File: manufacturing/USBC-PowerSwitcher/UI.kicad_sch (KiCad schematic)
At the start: 1 part, among them SW1 EC11N152440x

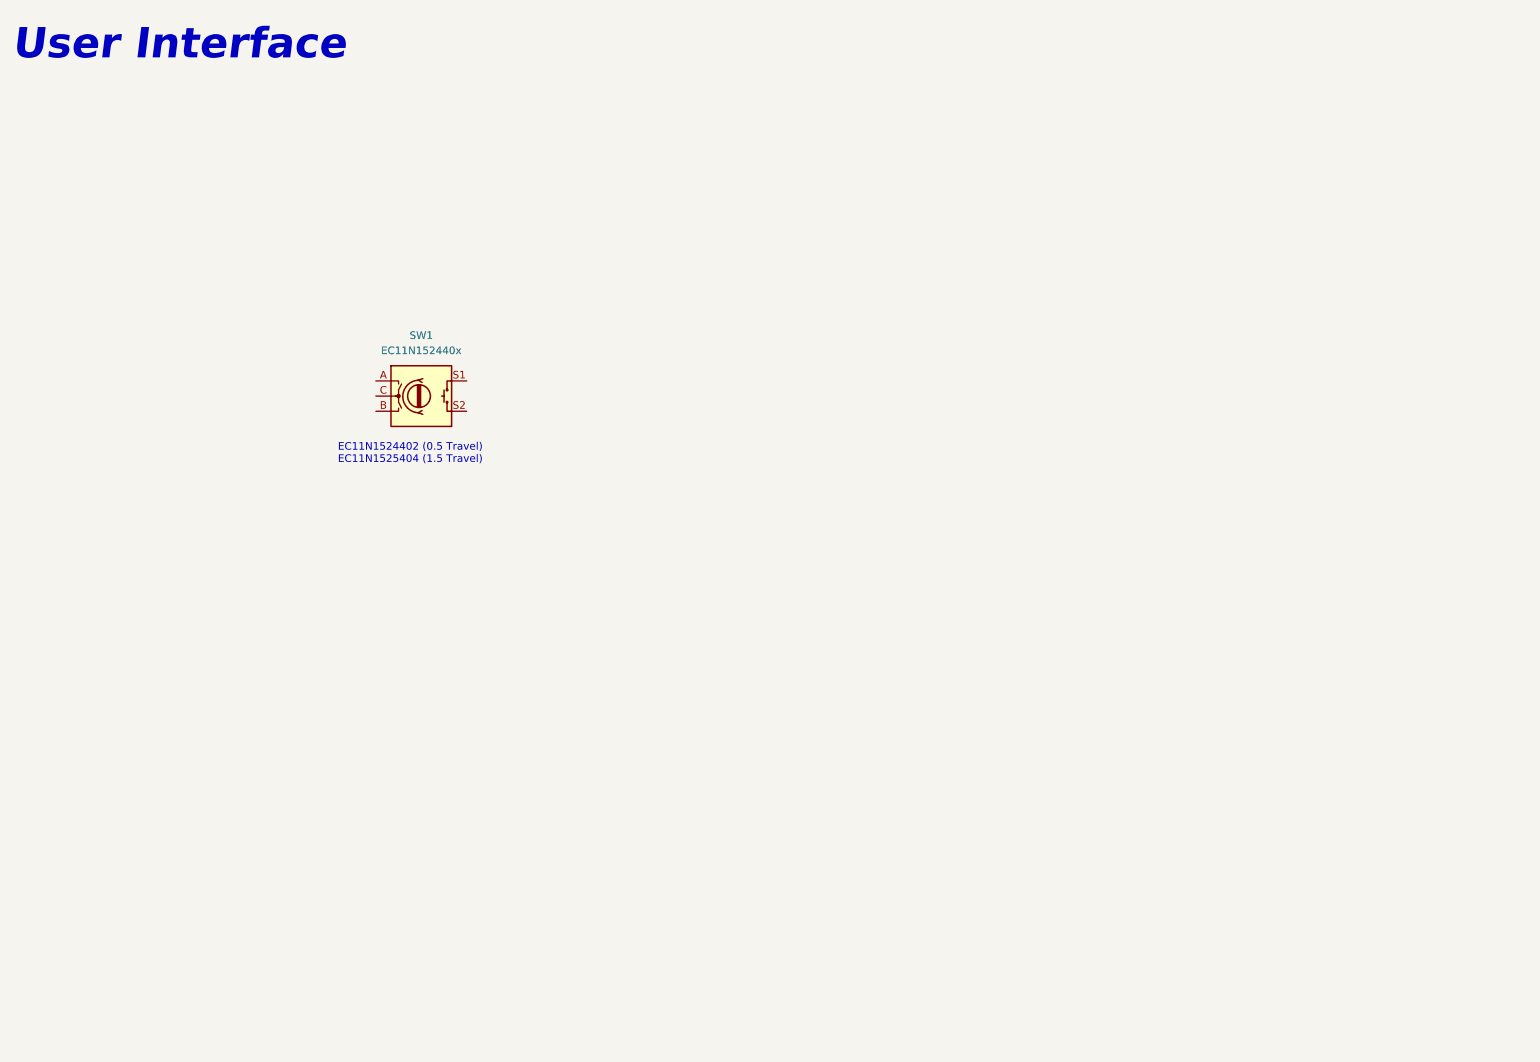
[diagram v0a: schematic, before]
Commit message: First Rough placement
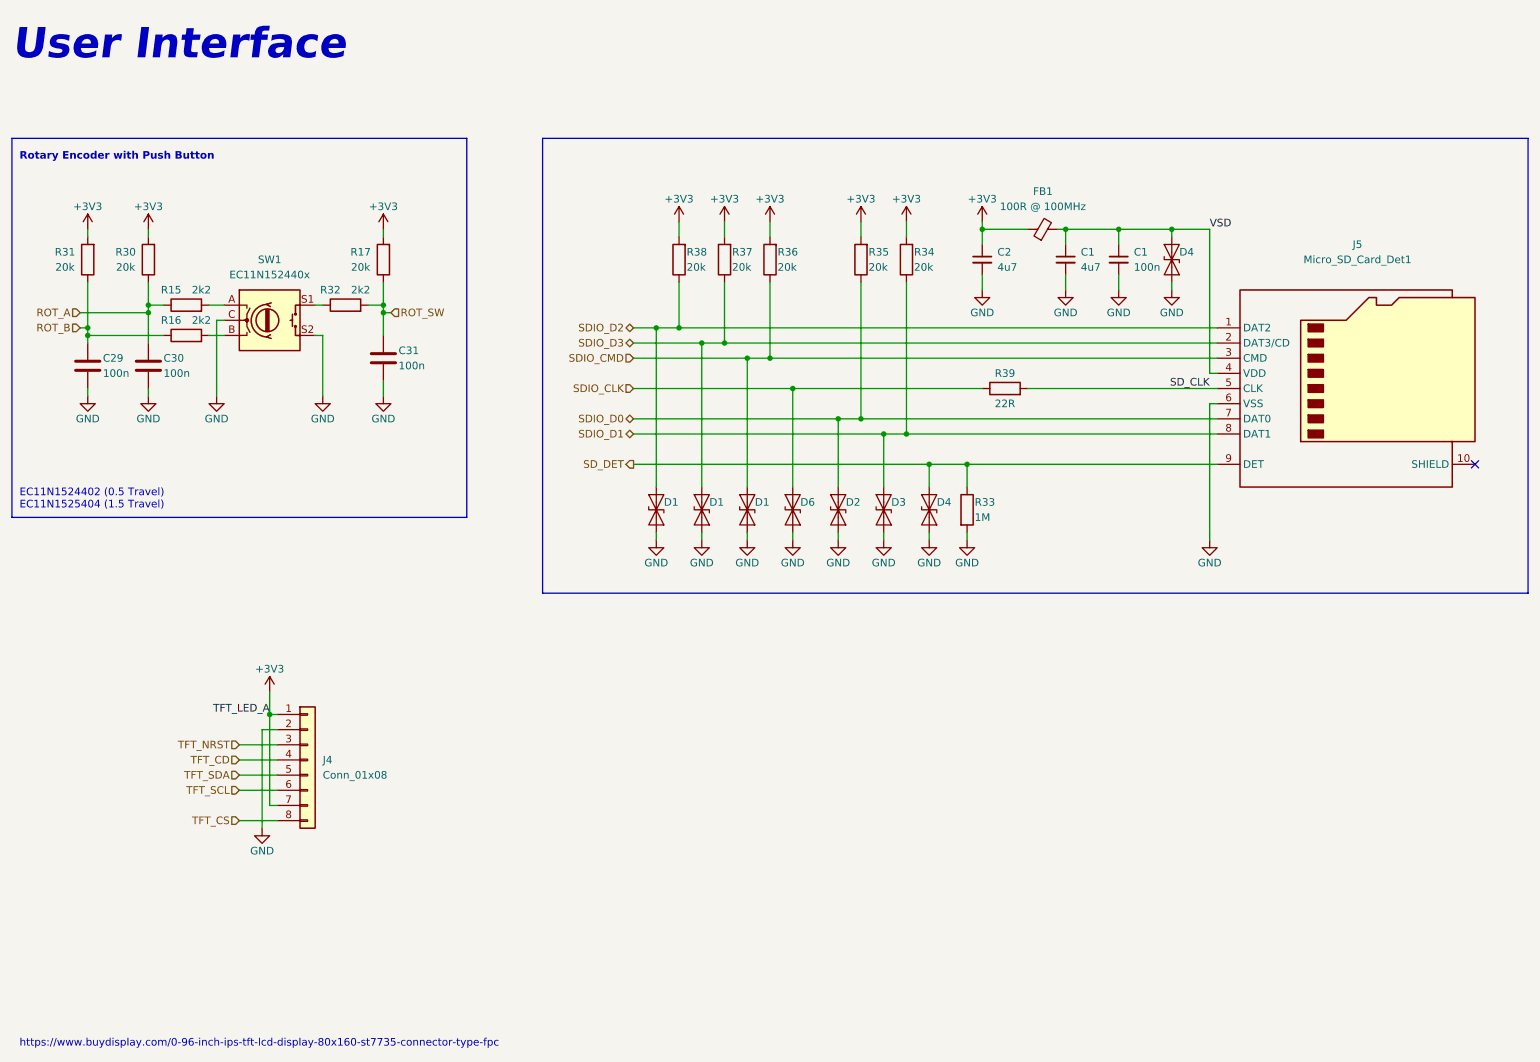
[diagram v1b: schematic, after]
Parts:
- added C1, C2: 4u7, Capacitor_SMD:C_0805_2012Metric, symbol Device:C_Small
- added C1: 100n, Capacitor_SMD:C_0402_1005Metric, symbol Device:C_Small
- added C29, C30, C31: 100n, Capacitor_SMD:C_0402_1005Metric, symbol Device:C
- added D1 (x3), D2, D3, D4 (x2), D6: ESD9B3.3ST5G, Diode_SMD:D_SOD-923, symbol Diode:ESD9B3.3ST5G
- added FB1: 100R @ 100MHz, Inductor_SMD:L_0805_2012Metric, symbol Device:FerriteBead_Small
- added J4: Conn_01x08, symbol Connector_Generic:Conn_01x08
- added J5: Micro_SD_Card_Det1, SamacSys_Parts:503398-1892, symbol Connector:Micro_SD_Card_Det1
- added R15, R16, R32: 2k2, Resistor_SMD:R_0402_1005Metric, symbol Device:R
- added R17, R30, R31, R34, R35, R36, R37, R38: 20k, Resistor_SMD:R_0402_1005Metric, symbol Device:R
- added R33: 1M, Resistor_SMD:R_0402_1005Metric, symbol Device:R
- added R39: 22R, Resistor_SMD:R_0402_1005Metric, symbol Device:R
- SW1: footprint (none) -> Rotary_Encoder:RotaryEncoder_Alps_EC11E-Switch_Vertical_H20mm; Mouser # (none) -> 688-EC11N1524402
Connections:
- net at SW1.A: now also R15.2
- net at SW1.B: now also R16.2
- net GND: now reaches SW1.C
- net GND: now also SW1.S2, C1.2, C1.2, C2.2, C29.2, C30.2, C31.2, D1.1 (A1), D1.1 (A1), D1.1 (A1), D2.1 (A1), D3.1 (A1), D4.1 (A1), D4.1 (A1), D6.1 (A1), J4.2 (Pin_2), J5.6 (VSS), R33.2
- net at SW1.S1: now also R32.1
- new net +3V3: C2.1, FB1.1, J4.1 (Pin_1), J4.7 (Pin_7), R17.2, R30.2, R31.2, R34.2, R35.2, R36.2, R37.2, R38.2
- new net ROT_A: C30.1, R15.1, R30.1
- new net ROT_B: C29.1, R16.1, R31.1
- new net ROT_SW: C31.1, R17.1, R32.2
- new net SDIO_CLK: D6.2 (A2), R39.1
- new net SDIO_CMD: D1.2 (A2), J5.3 (CMD), R36.1
- new net SDIO_D0: D2.2 (A2), J5.7 (DAT0), R35.1
- new net SDIO_D1: D3.2 (A2), J5.8 (DAT1), R34.1
- new net SDIO_D2: D1.2 (A2), J5.1 (DAT2), R38.1
- new net SDIO_D3: D1.2 (A2), J5.2 (DAT3/CD), R37.1
- new net SD_CLK: J5.5 (CLK), R39.2
- new net SD_DET: D4.2 (A2), J5.9 (DET), R33.1
- new net TFT_CD: J4.4 (Pin_4)
- new net TFT_CS: J4.8 (Pin_8)
- new net TFT_NRST: J4.3 (Pin_3)
- new net TFT_SCL: J4.6 (Pin_6)
- new net TFT_SDA: J4.5 (Pin_5)
- new net VSD: C1.1, C1.1, D4.2 (A2), FB1.2, J5.4 (VDD)
- no-connect marks 0 -> 1
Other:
- note added: "Rotary Encoder with Push Button"
- note added: "https://www.buydisplay.com/0-96-inch-ips-tft-lcd-display-80x160-st7735-connector-type-fpc"
- moved on the sheet: SW1
